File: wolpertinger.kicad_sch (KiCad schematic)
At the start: 92 parts, among them J1 RIGHT IN, J2 LEFT IN, J3 LEFT IN, J4 LEFT IN, J5 Jack-DC, K1 FRT5, K2 FRT5, Q1 BC549, Q2 2N5088, SW1 ON/OFF, U1 4093, U2 TL074, U3 TL074, U4 VTL5C, U5 VTL5C, U6 VTL5C, U7 VTL5C, U8 TL072, U9 L78L05_TO92

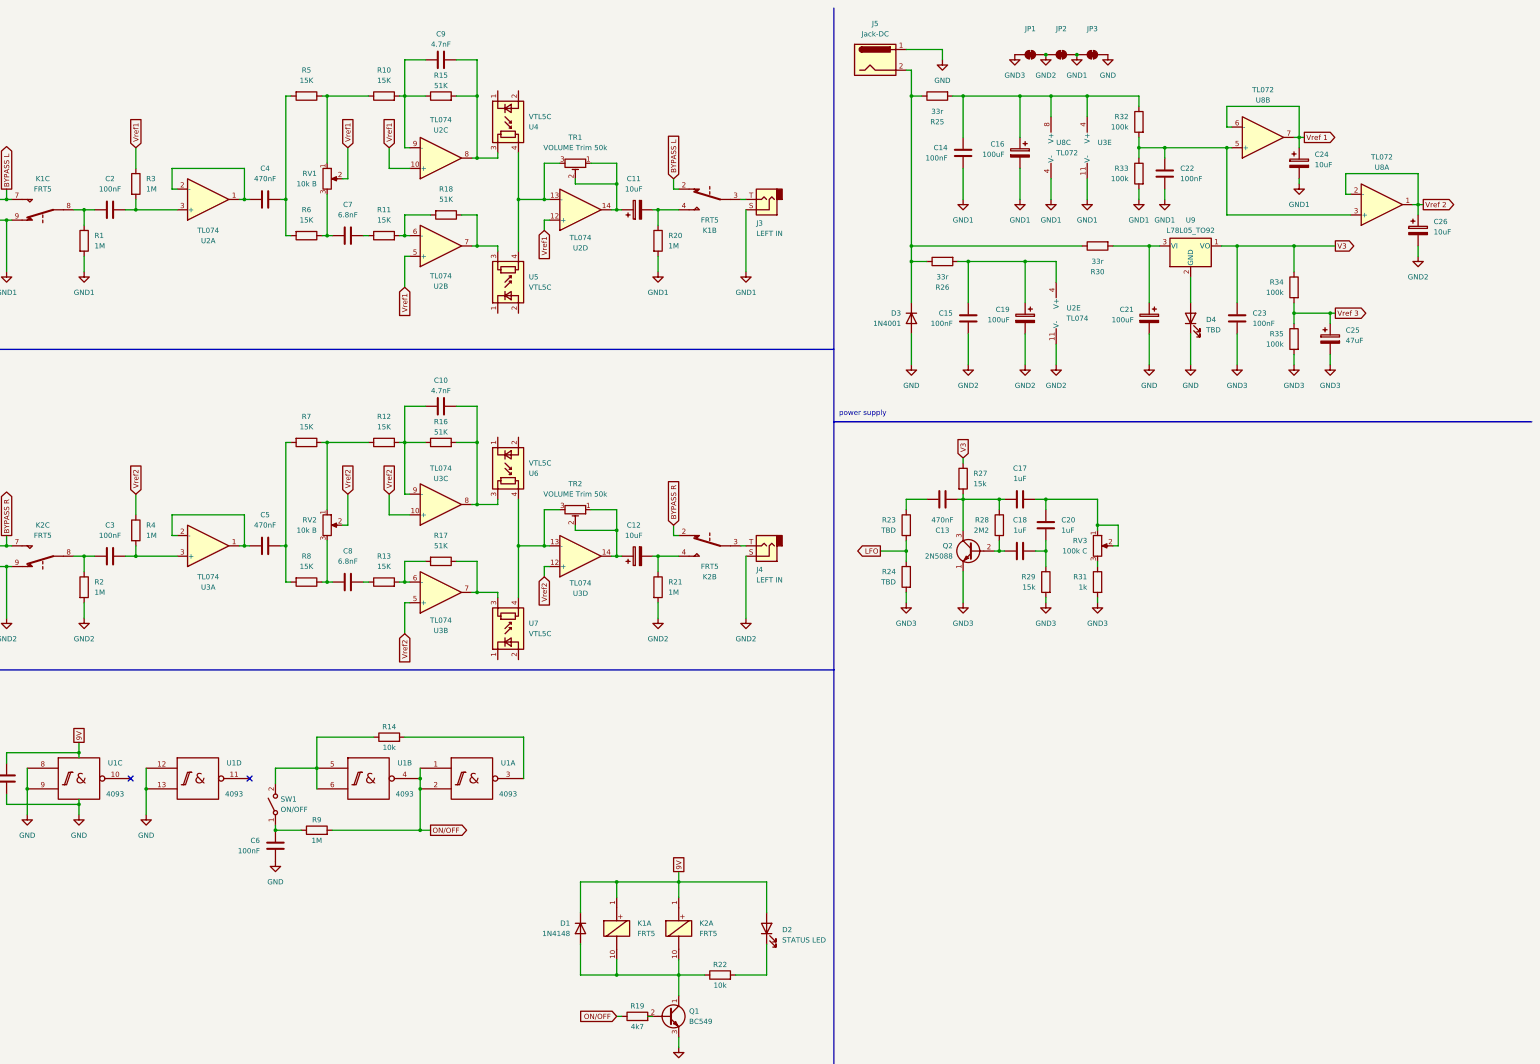
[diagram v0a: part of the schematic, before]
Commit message: cleanup power supply, add lfo voltage offset
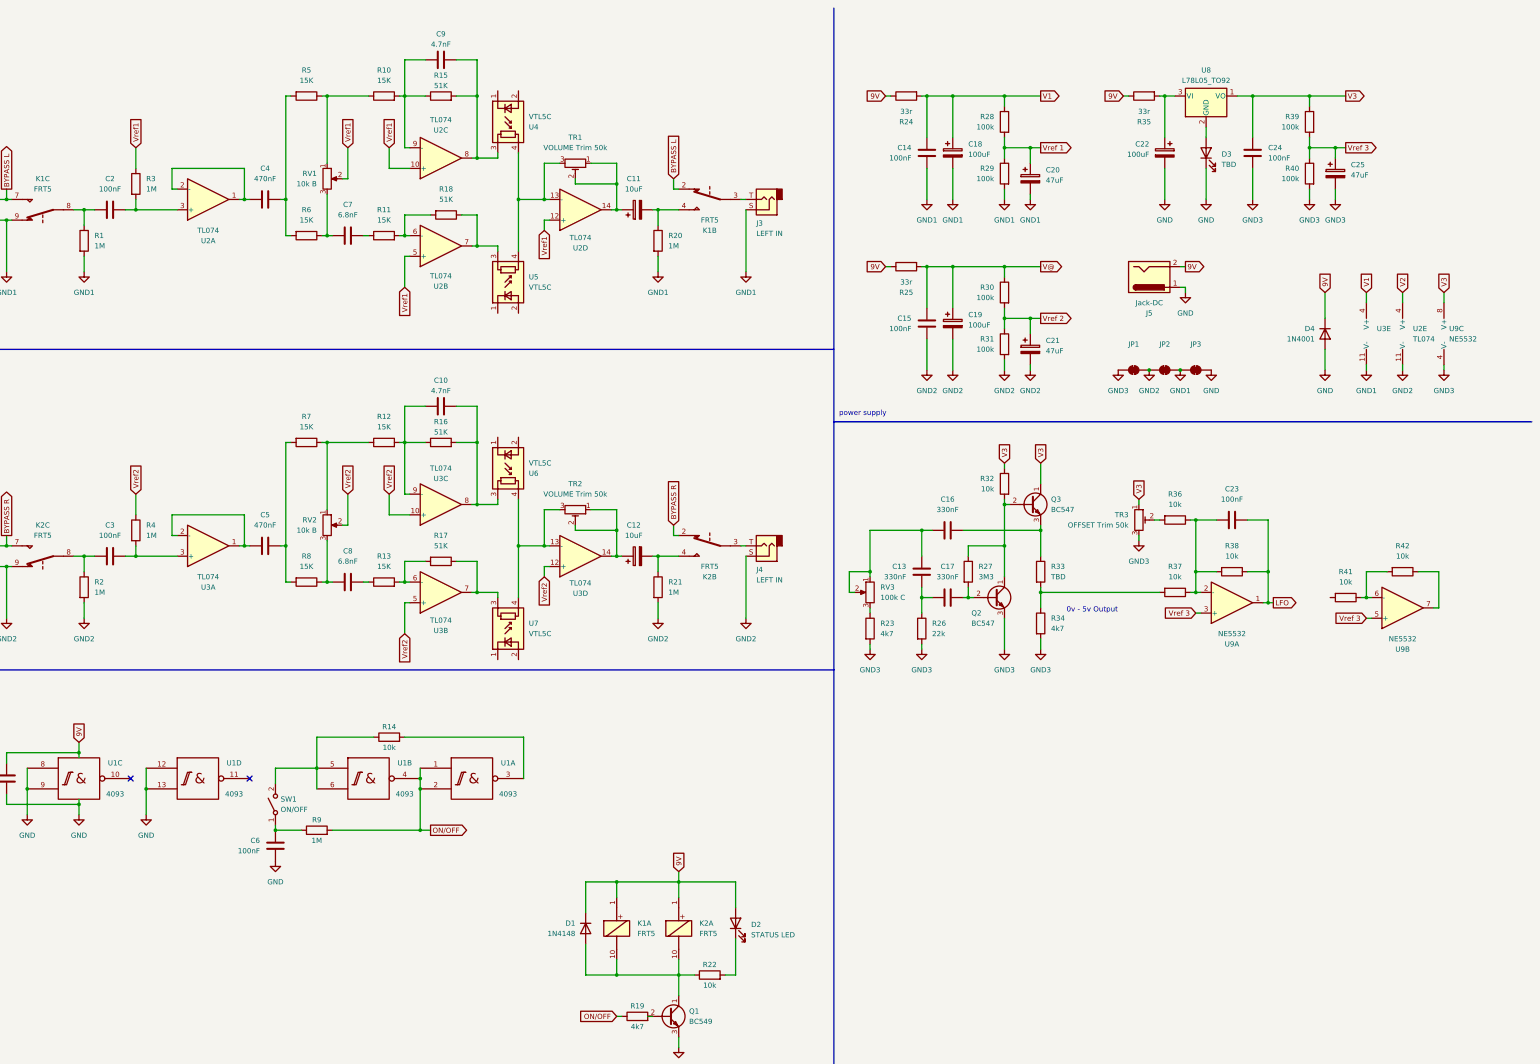
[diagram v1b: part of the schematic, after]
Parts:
- removed C13: 470nF, symbol Device:C
- removed C22: 100nF, symbol Device:C
- removed C26: 10uF, symbol Device:C_Polarized
- removed Q2: 2N5088, Package_TO_SOT_THT:TO-92_Inline, symbol Device:Q_NPN
- removed R26: 33r, Resistor_THT:R_Axial_DIN0207_L6.3mm_D2.5mm_P7.62mm_Horizontal, symbol Device:R
- removed U8: TL072, Package_DIP:DIP-8_W7.62mm_Socket_LongPads, symbol Amplifier_Operational:TL072
- added C21: 47uF, symbol Device:C_Polarized
- added C23: 100nF, symbol Device:C
- added Q2, Q3: BC547, Package_TO_SOT_THT:TO-92_Inline, symbol Transistor_BJT:BC547
- added R25: 33r, Resistor_THT:R_Axial_DIN0207_L6.3mm_D2.5mm_P7.62mm_Horizontal, symbol Device:R
- added R30, R31: 100k, Resistor_THT:R_Axial_DIN0207_L6.3mm_D2.5mm_P7.62mm_Horizontal, symbol Device:R
- added R36, R37, R38, R41, R42: 10k, Resistor_THT:R_Axial_DIN0207_L6.3mm_D2.5mm_P7.62mm_Horizontal, symbol Device:R
- added TR3: OFFSET Trim 50k, symbol Device:R_Potentiometer_Trim
- added U9: NE5532, Package_DIP:DIP-8_W7.62mm_Socket_LongPads, symbol Amplifier_Operational:NE5532
- C13: renamed from C20; value 1uF -> 330nF
- C16: renamed from C17; value 1uF -> 330nF
- C17: renamed from C18; value 1uF -> 330nF
- C20: renamed from C24; value 10uF -> 47uF
- R23: renamed from R31; value 1k -> 4k7
- R26: renamed from R29; value 15k -> 22k
- R27: renamed from R28; value 2M2 -> 3M3
- R32: renamed from R27; value 15k -> 10k
- R34: renamed from R24; value TBD -> 4k7
- renumbered C16 to C18, C21 to C22, C23 to C24, D4 to D3, D3 to D4, R25 to R24, R32 to R28, R33 to R29, R23 to R33, R30 to R35, R34 to R39, R35 to R40, U9 to U8
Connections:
- net GND2: now also C21.2, R31.2
- net GND3: now also Q2.3 (E), TR3.3, U9.4 (V-)
- net LFO: now also C23.1, R38.1, U9.1; no longer R33.2, R34.1
- net V3: now also Q3.1 (C), TR3.1, U9.8 (V+)
- net Vdd: now also D4.1 (K), J5.2, R24.1, R35.1, R25.1
- net Vref 1: now also R28.2, R29.1
- net Vref 2: now also C21.1, R30.2, R31.1
- net Vref 3: now also U9.3 (+), U9.5 (+)
- net at R27.1, R32.2: now also Q2.1 (C), Q3.2 (B); no longer C16.1
- net at C17.1, R27.2: now also Q2.2 (B)
- net V1: now reaches C14.2, C18.1, R24.2, R28.1, U3.4 (V+)
- net at R33.1: now also C16.1, Q3.3 (E)
- net V@: now reaches C15.2, C19.1
- net V@: now also R25.2, R30.1; no longer U2.4 (V+)
- new net: C23.2, R36.1, R37.1, R38.2, U9.2 (-)
- new net: R41.1, R42.2, U9.6 (-)
- new net: R42.1, U9.7
- new net: R33.2, R34.1, R37.2
- new net: R36.2, TR3.2
- new net V2: U2.4 (V+)
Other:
- note added: "0v - 5v Output"
- moved on the sheet: C13, C14, C16, C17, C18, C20, C22, C24, C25, D1, D2, D3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

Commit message: add custom part libary and add mode switch
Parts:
- added D1, D2: BAT42, Diode_THT:D_DO-35_SOD27_P7.62mm_Horizontal, symbol Diode:BAT42
- added J3: EXT LFO, symbol Connector_Audio:AudioJack2_SwitchT
- added R3: 10k, Resistor_THT:R_Axial_DIN0207_L6.3mm_D2.5mm_P7.62mm_Horizontal, symbol Device:R
- added R44, R45: 100r, Resistor_THT:R_Axial_DIN0207_L6.3mm_D2.5mm_P7.62mm_Horizontal, symbol Device:R
- added RV1: 100k B, symbol Device:R_Potentiometer
- added SW2: ~, switches:2P4T.MINI, symbol switches:2P4TMINIROTARY
- added TR4: LO R Trim 5k, symbol Device:R_Potentiometer_Trim
- added TR5: LO L Trim 5k, symbol Device:R_Potentiometer_Trim
- added TR6: HI R Trim 5k, symbol Device:R_Potentiometer_Trim
- added TR7: HI L Trim 5k, symbol Device:R_Potentiometer_Trim
- added U4: NE5532, Package_DIP:DIP-8_W7.62mm_Socket_LongPads, symbol Amplifier_Operational:NE5532
- J4: renamed from J3; value LEFT IN -> LEFT OUT
- J5: renamed from J4; value LEFT IN -> LEFT OUT
- TR3: value OFFSET Trim 50k -> OFFSET Trim 25k
- renumbered D1 to D3, D2 to D4, D3 to D5, D4 to D6, J5 to J6, R9 to R10, R10 to R11, R11 to R12, R12 to R13, R13 to R14, R14 to R15, R41 to R16, R15 to R17, R16 to R18, R17 to R19, R18 to R20, R42 to R21, R19 to R22, R20 to R23, R21 to R24, R22 to R25, R23 to R26, R24 to R27, R25 to R28, R26 to R29, R27 to R30, R28 to R31, R29 to R32, R30 to R33, R31 to R34, R32 to R35, R33 to R36, R34 to R37, R35 to R38, R36 to R39, R3 to R4, R37 to R40, R38 to R41, R39 to R42, R40 to R43, R4 to R5, R5 to R6, R6 to R7, R7 to R8, R8 to R9, RV1 to RV2, RV2 to RV3, RV3 to RV4, U8 to U10, U9 to U5, U4 to U6, U5 to U7, U6 to U8, U7 to U9
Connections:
- net V@ is gone; now on net V2: C15.2, C19.1, R28.2, R33.1
- net GND3: now also U6.1 (-), U7.1 (-), U8.1 (-), U9.1 (-), D2.2 (A), J3.S, U4.4 (V-)
- net LFO: now also J3.TN
- net V3: now also D1.1 (K), SW2.A4 (4), SW2.B3 (3), U4.8 (V+)
- net Vref 3: now also RV1.3
- net loL: now reaches U6.2 (+)
- net loL: now also TR5.3
- net LFO out inv: now reaches R16.2
- net LFO out inv: now also SW2.B2 (2), SW2.B4 (4), U4.6 (-), U4.7
- net LFO out: now reaches R21.1, U5.7
- net LFO out: now also SW2.A1 (1), SW2.A2 (2), SW2.A3 (3), SW2.B1 (1)
- net hiR: now reaches U9.2 (+)
- net hiR: now also TR6.3
- net loR: now reaches U8.2 (+)
- net loR: now also TR4.3
- net hiL: now reaches U7.2 (+)
- net hiL: now also TR7.3
- new net: R45.1, SW2.B (A)
- new net: R45.2, TR6.1, TR6.2
- new net: R44.1, SW2.A
- new net: R44.2, TR4.1, TR4.2
- new net: J3.T, R3.1
- new net: TR7.1, TR7.2
- new net: D1.2 (A), D2.1 (K), R3.2, RV1.1
- new net: RV1.2, U4.5 (+)
- new net: TR5.1, TR5.2
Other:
- moved on the sheet: C10, C11, C12, C2, C3, C4, C5, C7, C8, C9, D3, D4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

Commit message: remove hi and low only mode in favor of simpler switches
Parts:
- removed SW2: ~, switches:2P4T.MINI, symbol switches:2P4TMINIROTARY
- added R29, R36: 100r, Resistor_THT:R_Axial_DIN0207_L6.3mm_D2.5mm_P7.62mm_Horizontal, symbol Device:R
- added SW2: DPDT MONO/STEREO, symbol Switch:SW_DPDT_x2
- added SW3: DPDT HARMONIC/TREMOLO, symbol Switch:SW_DPDT_x2
- renumbered C14 to C13, C15 to C14, C18 to C15, C19 to C16, C20 to C17, C21 to C18, C13 to C19, C16 to C20, C17 to C21, C24 to C23, C25 to C24, C23 to C25, R17 to R16, R18 to R17, R19 to R18, R20 to R19, R16 to R20, R27 to R26, R28 to R27, R26 to R28, R4 to R3, R31 to R30, R32 to R31, R33 to R32, R34 to R33, R29 to R34, R30 to R35, R35 to R37, R36 to R39, R5 to R4, R37 to R40, R39 to R41, R40 to R42, R42 to R43, R43 to R44, R41 to R45, R44 to R46, R45 to R47, R3 to R5, TR5 to TR3, TR7 to TR4, TR3 to TR5, TR4 to TR6, TR6 to TR7, U6 to U5, U7 to U6, U8 to U7, U9 to U8, U5 to U9
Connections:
- net LFO out: now also SW2.3 (C), SW2.4 (A), SW3.3 (C)
- net LFO out inv: now also R47.1, SW2.1 (A), SW2.6 (C), SW3.1 (A)
- net at R46.1: now also SW3.2 (B)
- net at TR4.1, TR4.2: now also R36.2
- net at TR3.1, TR3.2: now also R29.2
- new net: R36.1, SW2.5 (B), SW3.4 (A)
- new net: R29.1, SW3.5 (B)
- new net: SW2.2 (B), SW3.6 (C)
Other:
- note added: "LDR config left"
- note added: "LDR config right"
- note added: "external LFO & LDR driver"
- note added: "onboard LFO"
- moved on the sheet: C19, C20, C21, C25, D1, D2, J3, Q2, Q3, R20, R21, R28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

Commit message: Add in mono to stereo out option
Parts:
- added C4: 10uF, symbol Device:C_Polarized
- renumbered C9 to C10, C10 to C11, C11 to C12, C12 to C13, C13 to C14, C14 to C15, C15 to C16, C16 to C17, C17 to C18, C18 to C19, C19 to C20, C20 to C21, C21 to C22, C22 to C23, C23 to C24, C24 to C25, C25 to C26, C4 to C5, C5 to C6, C6 to C7, C7 to C8, C8 to C9
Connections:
- net MONO IN: now also C4.2
- net at C5.1, U2.1, U2.2 (-): now also C4.1
- no-connect marks 3 -> 6
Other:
- note added: "mono/left channel"
- note removed: "left channel"
- moved on the sheet: R10, R15

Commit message: Add Footprints pt1
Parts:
- RV1, RV2, RV3, RV4: footprint (none) -> potentiometers:16MM_PADS.1
- SW1: footprint (none) -> switches:SPST
- SW2, SW3: footprint (none) -> switches:DPDT
- TR1, TR2, TR3, TR4, TR5, TR6, TR7: footprint (none) -> Potentiometer_THT:Potentiometer_Piher_PT-6-V_Vertical
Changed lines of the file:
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@@
 			)
 		)
-		(property "Footprint" ""
+		(property "Footprint" "switches:DPDT"
 			(at 360.68 214.63 0)
 			(effects
@@
 			)
 		)
-		(property "Footprint" ""
+		(property "Footprint" "switches:SPST"
 			(at 99.06 208.28 0)
 			(effects
@@
 			)
 		)
-		(property "Footprint" ""
+		(property "Footprint" "Potentiometer_THT:Potentiometer_Piher_PT-6-V_Vertical"
 			(at 172.72 132.08 0)
 			(effects
@@
 			)
 		)
-		(property "Footprint" ""
+		(property "Footprint" "switches:DPDT"
 			(at 298.45 201.93 0)
 			(effects
@@
 			)
 		)
-		(property "Footprint" ""
+		(property "Footprint" "potentiometers:16MM_PADS.1"
 			(at 271.78 156.21 0)
 			(effects
@@
 			)
 		)
-		(property "Footprint" ""
+		(property "Footprint" "Potentiometer_THT:Potentiometer_Piher_PT-6-V_Vertical"
 			(at 388.62 236.22 0)
 			(effects
@@
 			)
 		)
-		(property "Footprint" ""
+		(property "Footprint" "Potentiometer_THT:Potentiometer_Piher_PT-6-V_Vertical"
 			(at 298.45 236.22 0)
 			(effects
@@
 			)
 		)
-		(property "Footprint" ""
+		(property "Footprint" "potentiometers:16MM_PADS.1"
 			(at 99.06 265.43 0)
 			(effects
@@
 			)
 		)
-		(property "Footprint" ""
+		(property "Footprint" "switches:DPDT"
 			(at 271.78 201.93 0)
 			(effects
@@
 			)
 		)
-		(property "Footprint" ""
+		(property "Footprint" "potentiometers:16MM_PADS.1"
 			(at 111.76 50.8 0)
 			(effects
@@
 			)
 		)
-		(property "Footprint" ""
+		(property "Footprint" "Potentiometer_THT:Potentiometer_Piher_PT-6-V_Vertical"
 			(at 360.68 236.22 0)
 			(effects
@@
 			)
 		)
-		(property "Footprint" ""
+		(property "Footprint" "potentiometers:16MM_PADS.1"
 			(at 111.76 135.89 0)
 			(effects
@@
 			)
 		)
-		(property "Footprint" ""
+		(property "Footprint" "Potentiometer_THT:Potentiometer_Piher_PT-6-V_Vertical"
 			(at 337.82 138.43 0)
 			(effects
@@
 			)
 		)
-		(property "Footprint" ""
+		(property "Footprint" "switches:DPDT"
 			(at 274.32 214.63 0)
 			(effects
@@
 			)
 		)
-		(property "Footprint" ""
+		(property "Footprint" "Potentiometer_THT:Potentiometer_Piher_PT-6-V_Vertical"
 			(at 172.72 46.99 0)
 			(effects
@@
 			)
 		)
-		(property "Footprint" ""
+		(property "Footprint" "Potentiometer_THT:Potentiometer_Piher_PT-6-V_Vertical"
 			(at 274.32 236.22 0)
 			(effects

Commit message: Add DC Jk Footprint
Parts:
- J6: footprint (none) -> jacks:BATTERY
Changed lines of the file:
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@@
 			)
 		)
-		(property "Footprint" ""
+		(property "Footprint" "jacks:BATTERY"
 			(at 314.96 77.724 0)
 			(effects
